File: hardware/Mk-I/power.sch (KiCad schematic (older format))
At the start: 14 parts, among them CON1 10118194-0001LF, U2 MCP73831T-2ACI/OT, U3 BD33IA5MEFJ-ME2

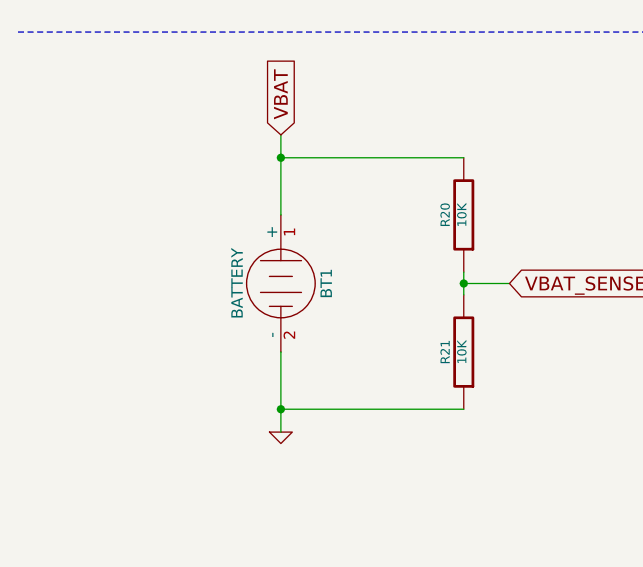
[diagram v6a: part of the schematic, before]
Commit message: HW: Change battery connector to SMD
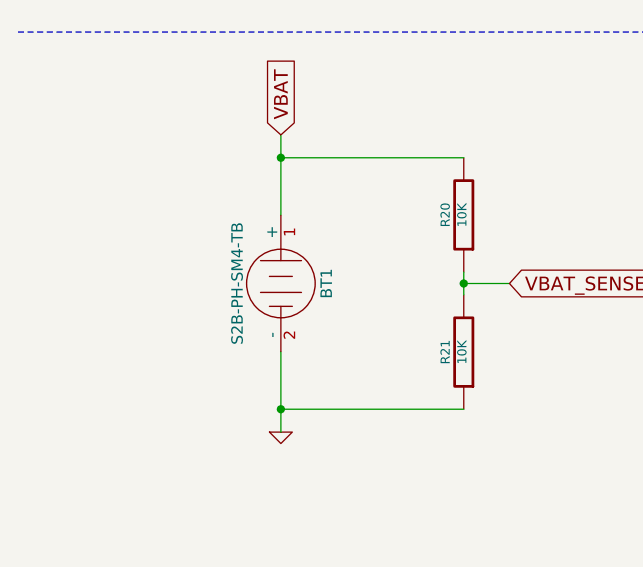
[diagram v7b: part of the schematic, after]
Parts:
- BT1: value BATTERY -> S2B-PH-SM4-TB; footprint Connect:PINHEAD1-2 -> Connectors_JST:JST_PH_S2B-PH-SM4-TB_02x2.00mm_Angled
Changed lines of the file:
@@
 P 1650 4400
 F 0 "BT1" H 1650 4600 50  0000 C CNN
-F 1 "BATTERY" H 1650 4210 50  0000 C CNN
-F 2 "Connect:PINHEAD1-2" H 1650 4400 60  0001 C CNN
+F 1 "S2B-PH-SM4-TB" H 1650 4210 50  0000 C CNN
+F 2 "Connectors_JST:JST_PH_S2B-PH-SM4-TB_02x2.00mm_Angled" H 1650 4400 60  0001 C CNN
 F 3 "" H 1650 4400 60  0000 C CNN
 	1    1650 4400
